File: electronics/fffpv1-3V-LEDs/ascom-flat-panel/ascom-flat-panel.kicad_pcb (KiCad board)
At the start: 2 copper layers, 56 x 32 mm, 14 parts, among them J1 Servo, J2 JST-XH LED, Q1 IRLZ34N, Q2 IRLZ34N, U1 XIAO-SAMD21-DIP

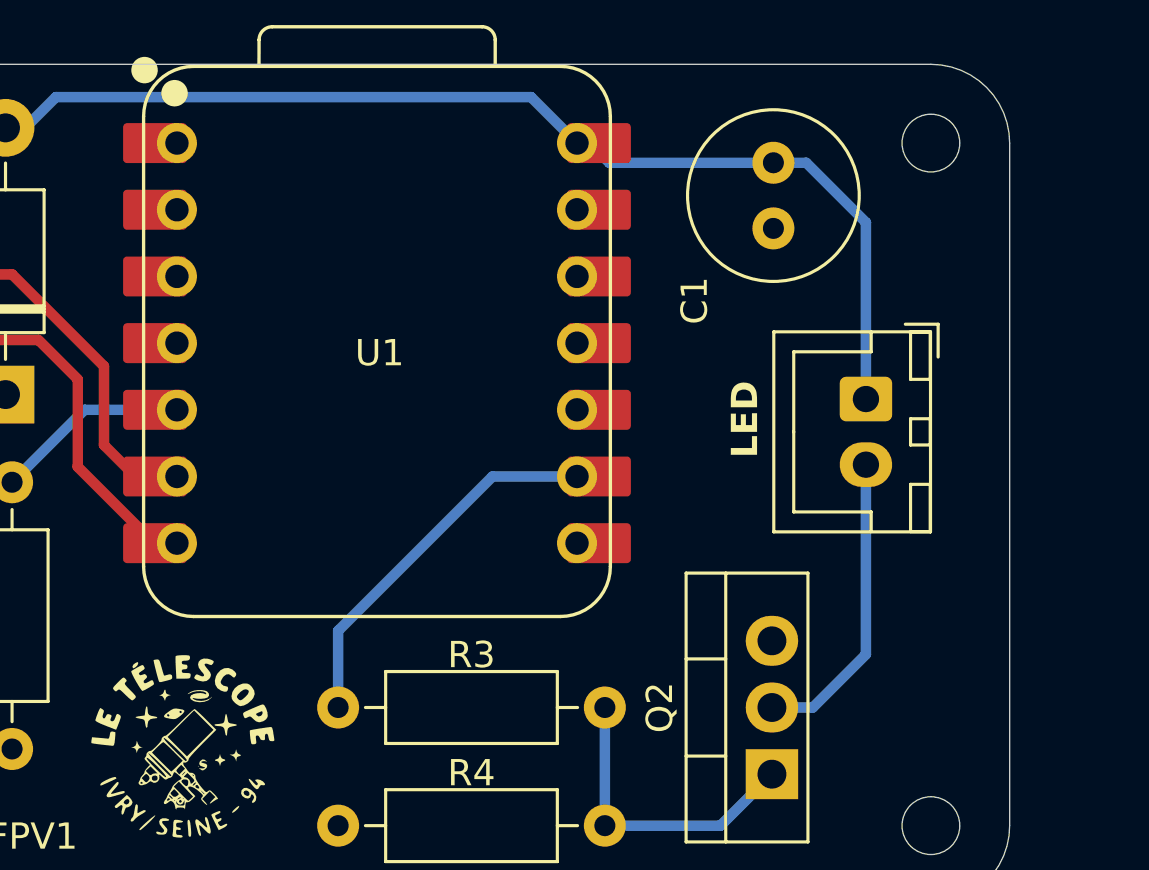
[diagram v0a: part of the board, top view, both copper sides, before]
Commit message: [circuit] PCB modified accordingly to schematics
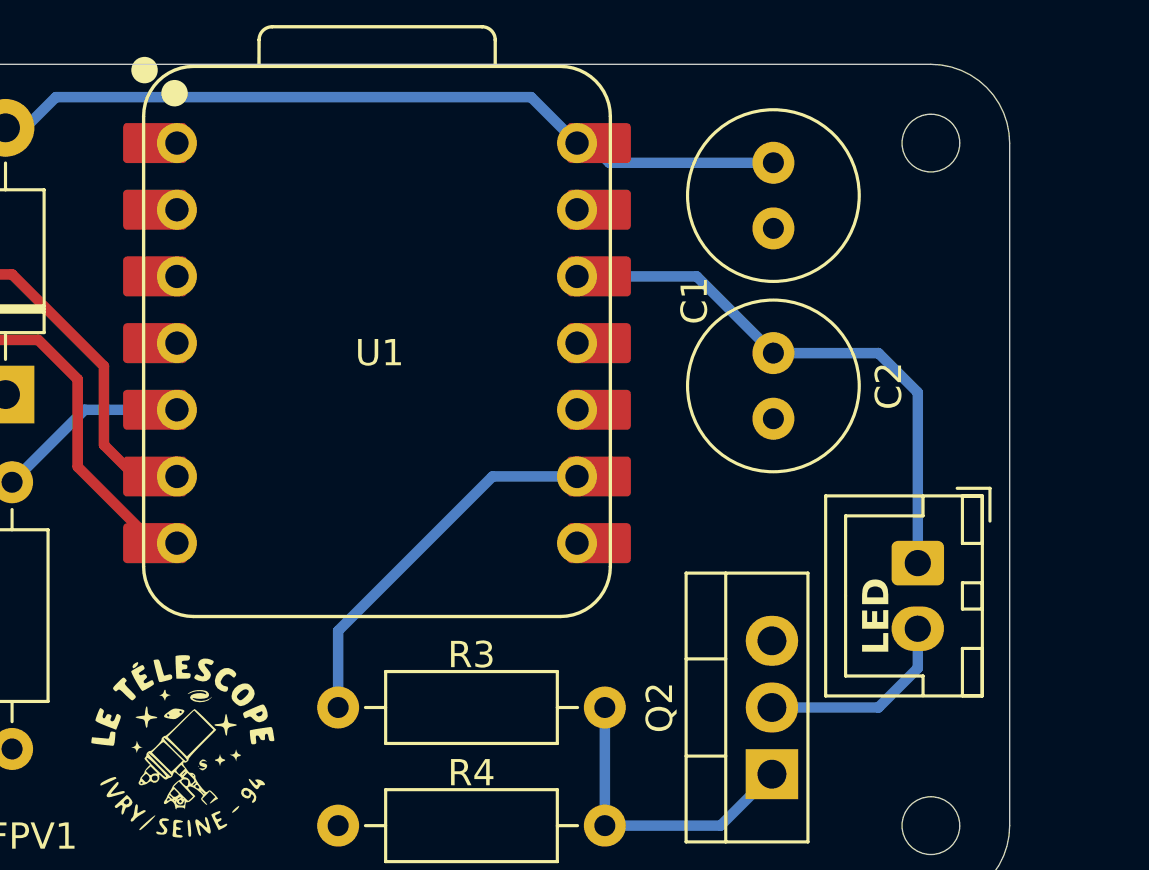
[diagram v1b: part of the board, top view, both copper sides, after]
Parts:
- added C2: 10µF, Capacitor_THT:C_Radial_D6.3mm_H11.0mm_P2.50mm, F.Cu at (143.0, 81.0)
- moved J2 6.55 mm to (148.5, 89.0)
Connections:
- J2 pad 1: +5V -> +3V3
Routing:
- net +3V3: track 0.00 -> 21.3 mm
- net +5V: track 41.2 -> 30.0 mm
- net Net-(J2-Pin_2): track 11.6 -> 7.68 mm
- net SERVO POSITION FEEDBACK: track 22.5 -> 22.0 mm
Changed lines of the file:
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@@
 			(psa4output no)
 			(plot_black_and_white yes)
-			(plotinvisibletext no)
 			(sketchpadsonfab no)
 			(plotpadnumbers no)
@@
 		)
 	)
+	(footprint "Capacitor_THT:C_Radial_D6.3mm_H11.0mm_P2.50mm"
+		(layer "F.Cu")
+		(at 143 81 -90)
+		(descr "C, Radial series, Radial, pin pitch=2.50mm, diameter=6.3mm, height=11mm, Non-Polar Electrolytic Capacitor")
+		(tags "C Radial series Radial pin pitch 2.50mm diameter 6.3mm height 11mm Non-Polar Electrolytic Capacitor")
+		(property "Reference" "C2"
+			(at 1.25 -4.4 90)
+			(layer "F.SilkS")
+			(effects
+				(font
+					(size 1 1)
+					(thickness 0.15)
+				)
+			)
+		)
+		(property "Value" "10µF"
+			(at 1.25 4.4 90)
+			(layer "F.Fab")
+			(effects
+				(font
+					(size 1 1)
+					(thickness 0.15)
+				)
+			)
+		)
+		(property "Datasheet" ""
+			(at 0 0 90)
+			(layer "F.Fab")
+			(hide yes)
+			(effects
+				(font
+					(size 1.27 1.27)
+					(thickness 0.15)
+				)
+			)
+		)
+		(property "Description" ""
+			(at 0 0 90)
+			(layer "F.Fab")
+			(hide yes)
+			(effects
+				(font
+					(size 1.27 1.27)
+					(thickness 0.15)
+				)
+			)
+		)
+		(property ki_fp_filters "CP_*")
+		(sheetname "/")
+		(sheetfile "ascom-flat-panel.kicad_sch")
+		(attr through_hole)
+		(fp_circle
+			(center 1.25 0)
+			(end 4.52 0)
+			(stroke
+				(width 0.12)
+				(type solid)
+			)
+			(fill no)
+			(layer "F.SilkS")
+		)
+		(fp_circle
+			(center 1.25 0)
+			(end 4.65 0)
+			(stroke
+				(width 0.05)
+				(type solid)
+			)
+			(fill no)
+			(layer "F.CrtYd")
+		)
+		(fp_circle
+			(center 1.25 0)
+			(end 4.4 0)
+			(stroke
+				(width 0.1)
+				(type solid)
+			)
+			(fill no)
+			(layer "F.Fab")
+		)
+		(fp_text user "${REFERENCE}"
+			(at 1.25 0 90)
+			(layer "F.Fab")
+			(effects
+				(font
+					(size 1 1)
+					(thickness 0.15)
+				)
+			)
+		)
+		(pad "1" thru_hole circle
+			(at 0 0 270)
+			(size 1.6 1.6)
+			(drill 0.8)
+			(layers "*.Cu" "*.Mask")
+			(remove_unused_layers no)
+			(net 7 "+3V3")
+			(pintype "passive")
+		)
+		(pad "2" thru_hole circle
+			(at 2.5 0 270)
+			(size 1.6 1.6)
+			(drill 0.8)
+			(layers "*.Cu" "*.Mask")
+			(remove_unused_layers no)
+			(net 1 "GND")
+			(pintype "passive")
+		)
+		(embedded_fonts no)
+		(model "${KICAD9_3DMODEL_DIR}/Capacitor_THT.3dshapes/C_Radial_D6.3mm_H11.0mm_P2.50mm.wrl"
+			(offset
+				(xyz 0 0 0)
+			)
+			(scale
+				(xyz 1 1 1)
+			)
+			(rotate
+				(xyz 0 0 0)
+			)
+		)
+	)
 	(footprint "Diode_THT:D_DO-41_SOD81_P10.16mm_Horizontal"
 		(layer "F.Cu")
@@
 	(footprint "Connector_JST:JST_XH_B2B-XH-A_1x02_P2.50mm_Vertical"
 		(layer "F.Cu")
-		(at 146.525 82.75 -90)
+		(at 148.5 89 -90)
 		(descr "JST XH series connector, B2B-XH-A (http://www.jst-mfg.com/product/pdf/eng/eXH.pdf), generated with kicad-footprint-generator")
 		(tags "connector JST XH vertical")
@@
 		)
 		(property "Value" "JST-XH LED"
-			(at 1.25 4.6 90)
+			(at 1.25 -1.5 90)
 			(layer "F.Fab")
 			(effects
@@
 			(remove_unused_layers no)
 			(roundrect_rratio 0.147059)
-			(net 2 "+5V")
+			(net 7 "+3V3")
 			(pinfunction "Pin_1")
 			(pintype "passive")
@@
 	)
 	(gr_text "LED"
-		(at 142.5 85 90)
+		(at 147.5 92.5 90)
 		(layer "F.SilkS")
 		(effects
@@
 	)
 	(segment
-		(start 143 73.75)
-		(end 144.25 73.75)
-		(width 0.4)
-		(layer "B.Cu")
-		(net 2)
-	)
-	(segment
 		(start 136.75 73.75)
 		(end 143 73.75)
@@
 	)
 	(segment
-		(start 146.525 76.025)
-		(end 146.525 82.75)
-		(width 0.4)
-		(layer "B.Cu")
-		(net 2)
-	)
-	(segment
 		(start 135.52 73)
 		(end 136 73)
@@
 	)
 	(segment
-		(start 144.25 73.75)
-		(end 146.525 76.025)
-		(width 0.4)
-		(layer "B.Cu")
-		(net 2)
-	)
-	(segment
 		(start 109 82.08)
 		(end 109 77.8)
@@
 	)
 	(segment
-		(start 120.28 88.24)
-		(end 119.74 88.24)
-		(width 0.4)
-		(layer "B.Cu")
-		(net 5)
-	)
-	(segment
 		(start 120.28 85.7)
 		(end 118.7 85.7)
@@
 	)
 	(segment
-		(start 144.5 94.5)
-		(end 142.945 94.5)
+		(start 148.5 82.5)
+		(end 148.5 89)
+		(width 0.4)
+		(layer "B.Cu")
+		(net 7)
+	)
+	(segment
+		(start 147 81)
+		(end 148.5 82.5)
+		(width 0.4)
+		(layer "B.Cu")
+		(net 7)
+	)
+	(segment
+		(start 143 81)
+		(end 147 81)
+		(width 0.4)
+		(layer "B.Cu")
+		(net 7)
+	)
+	(segment
+		(start 140.08 78.08)
+		(end 143 81)
+		(width 0.4)
+		(layer "B.Cu")
+		(net 7)
+	)
+	(segment
+		(start 135.52 78.08)
+		(end 140.08 78.08)
+		(width 0.4)
+		(layer "B.Cu")
+		(net 7)
+	)
+	(segment
+		(start 148.5 91.5)
+		(end 148.5 93)
 		(width 0.4)
 		(layer "B.Cu")
@@
 	)
 	(segment
-		(start 146.525 85.25)
-		(end 146.525 92.475)
+		(start 147 94.5)
+		(end 142.945 94.5)
 		(width 0.4)
 		(layer "B.Cu")
@@
 	)
 	(segment
-		(start 146.525 92.475)
-		(end 144.5 94.5)
+		(start 148.5 93)
+		(end 147 94.5)
 		(width 0.4)
 		(layer "B.Cu")
